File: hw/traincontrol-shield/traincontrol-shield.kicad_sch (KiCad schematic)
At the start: 3 parts, among them J4 Track Input, J5 Motor Windings, J6 Motor+AC

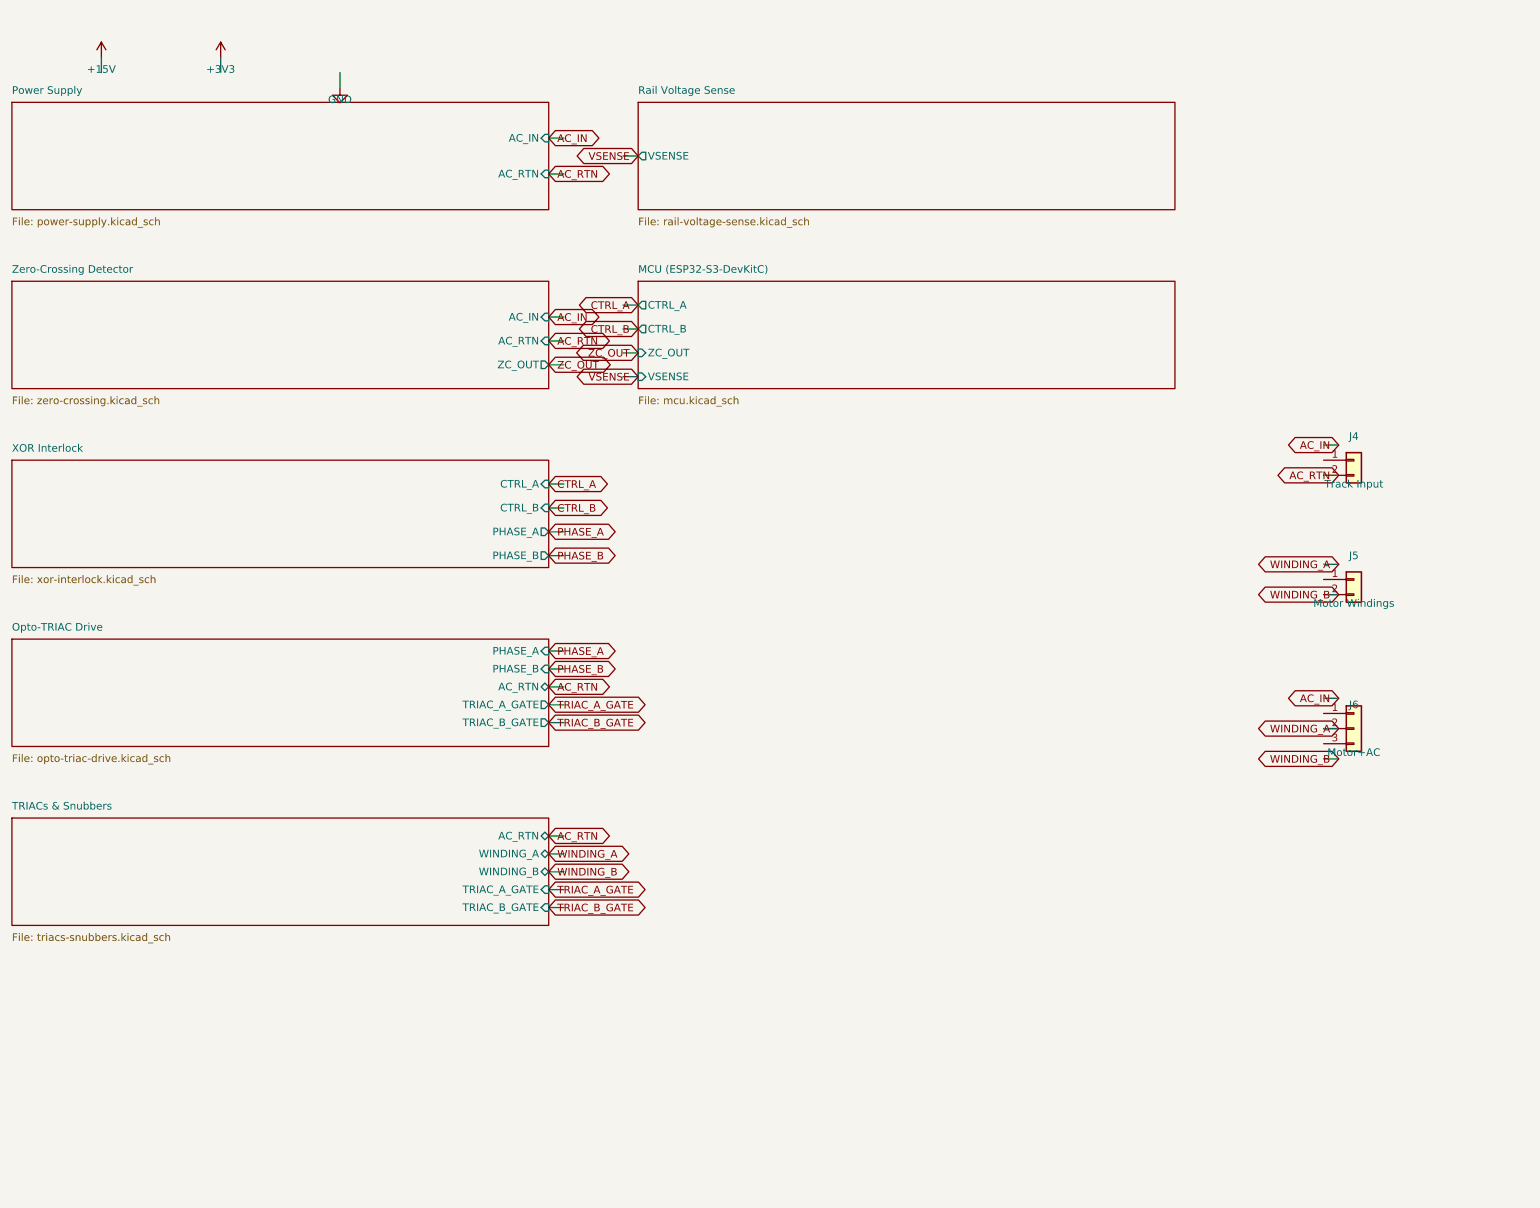
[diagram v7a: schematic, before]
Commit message: Disperse component layout and triple wire stub length across all sheets
- STUB: 2.54 → 7.62 mm (3×) in all three generator scripts
- Inter-component spacing doubled in power-supply, MCU, and logic sheets
- Top-level inter-column gap widened (LX 120 → 130 mm) to avoid label collision
- Sheet frame heights made variable per pin count (20–35 mm)
- Right-column sheet x-origin and connector J4/J5/J6 x-positions updated accordingly
- All 8 sheets regenerated and validated with kicad-cli

Co-Authored-By: Claude Sonnet 4.6 <noreply@anthropic.com>
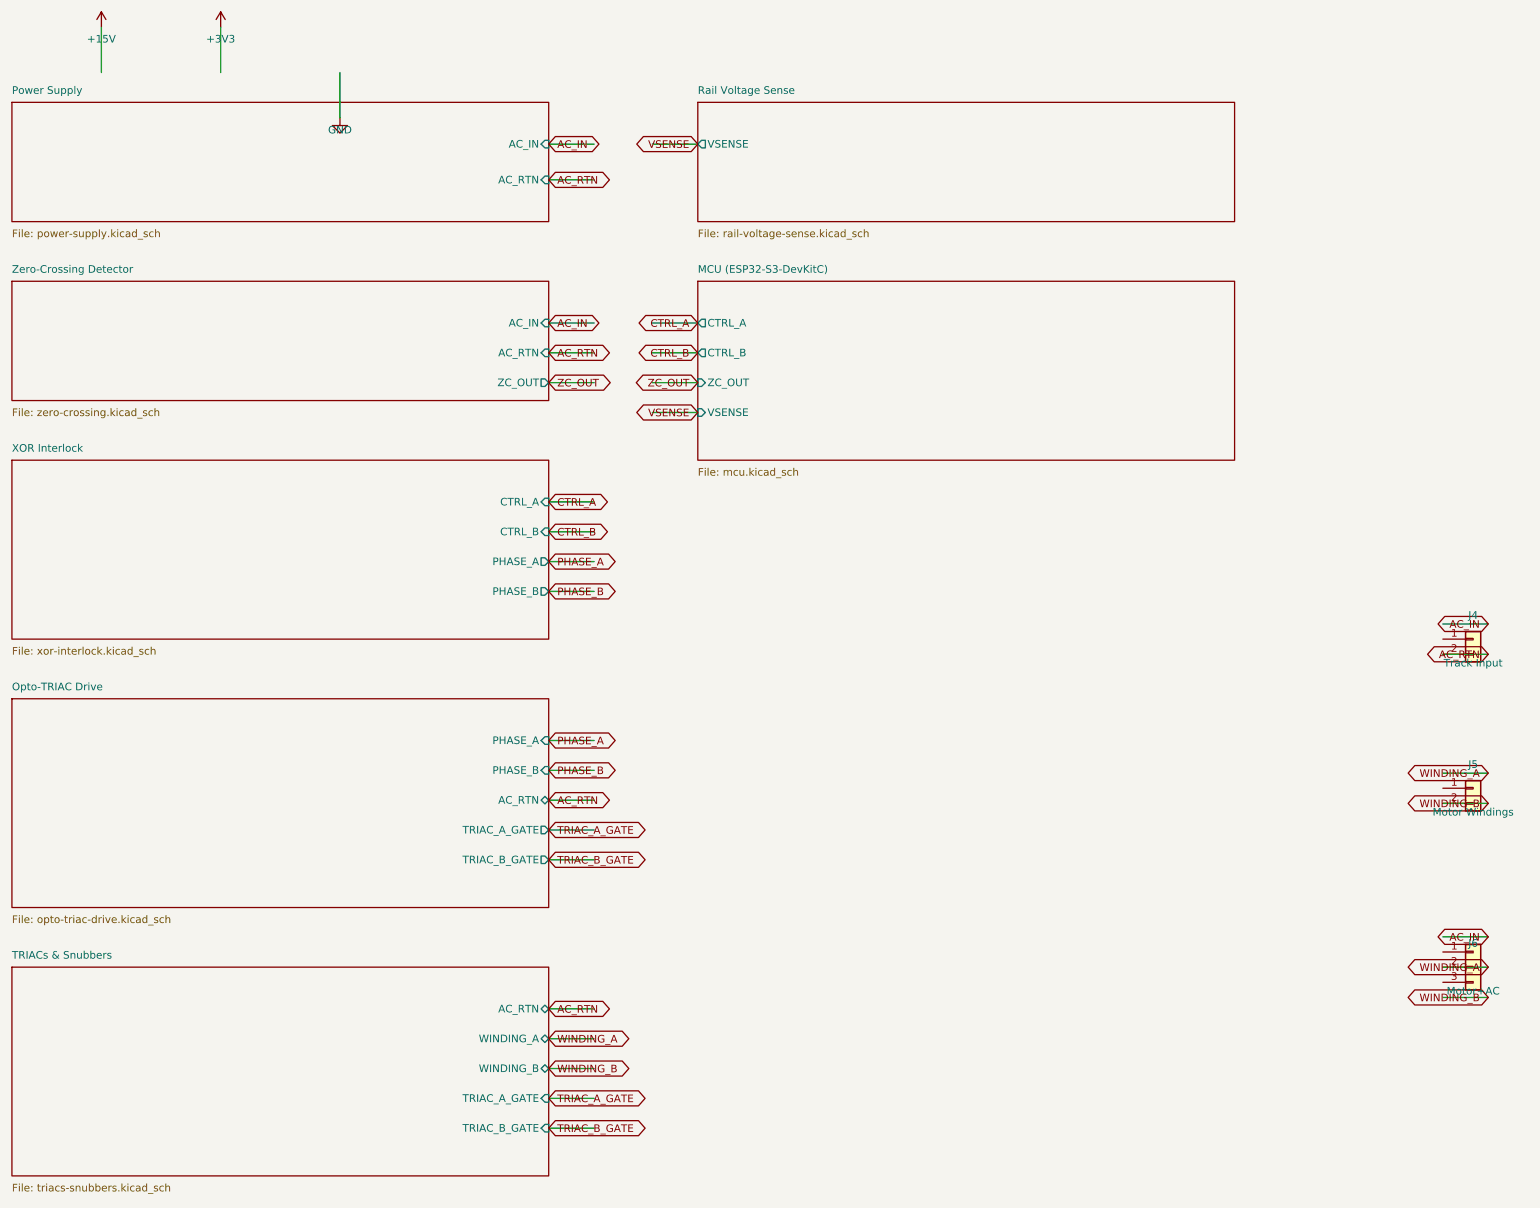
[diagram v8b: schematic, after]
